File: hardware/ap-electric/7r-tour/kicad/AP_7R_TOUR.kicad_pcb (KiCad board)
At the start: 2 copper layers, 176 x 90 mm, 185 parts, among them J1 KF128-5.08-2P, J11 KF128-5.08-3P, J12 KF128-5.08-3P, J13 KF128-5.08-3P, J14 KF128-5.08-3P, J15 USB-C, J2 KF128-5.08-2P, J3 KF128-5.08-2P, J4 KF128-5.08-2P, J5 KF128-5.08-2P, J6 KF128-5.08-2P, J7 KF128-5.08-2P, J8 KF128-5.08-2P, J9 KF128-5.08-2P, K1 G2RL-1A-E DC24, K2 G2RL-1A-E DC24, K3 G2RL-1A-E DC24, K4 G2RL-1A-E DC24, K5 G2RL-1A-E DC24, K6 G2RL-1A-E DC24, K7 G2RL-1A-E DC24, SW1 DSWB08LHGET, SW8 MODO, SW9 RESET, U1 ULN2003ADR, U10 USBLC6-2SC6, U2 TCA9554PWR, U3 TCA9554PWR, U4 TCA9554PWR, U5 TCA9554PWR, U6 CA-IS3092W, U7 LMR16006XDDC, U8 AP63203WU, U9 ESP32-C3-WROOM-02

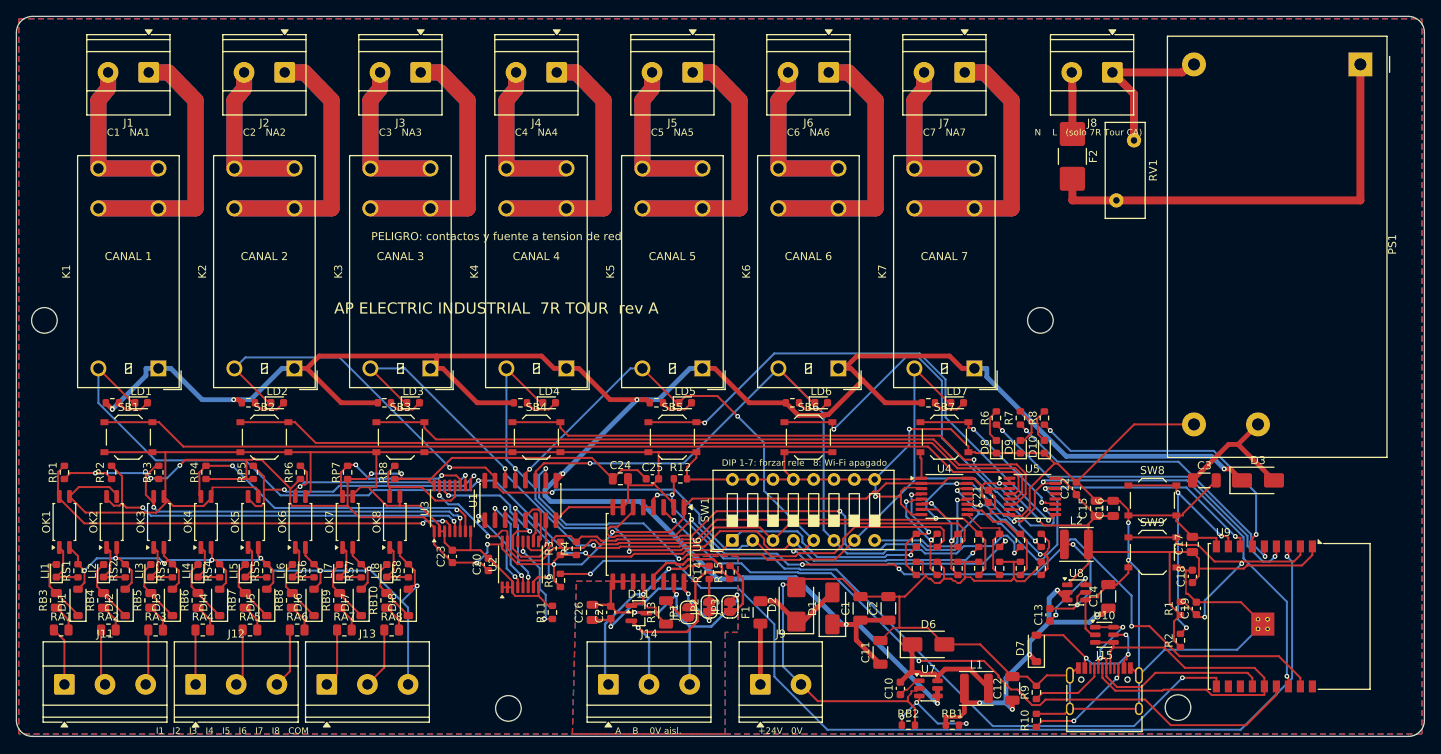
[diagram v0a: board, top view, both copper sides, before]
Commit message: 7R Tour: placa cerrada (DRC 0) y salidas de fabricación por SKU
Ruteo completo con el bus aislado trazado a mano: 0 violaciones,
0 sin conectar, paridad 0, DFM de JLCPCB 0. Gerbers, taladros,
BOM y CPL; BOM/CPL separados para 7R Tour 24DC y 7R Tour CA.
Código verificado del borne KF128-5.08-3P para su huella. LEEME
del 7R Tour con el estado de cierre y los pendientes.

Co-Authored-By: Claude Opus 5.5 <noreply@anthropic.com>
Claude-Session: https://claude.ai/code/session_01WVk3oGwfQfGTmAT2PMp8oW
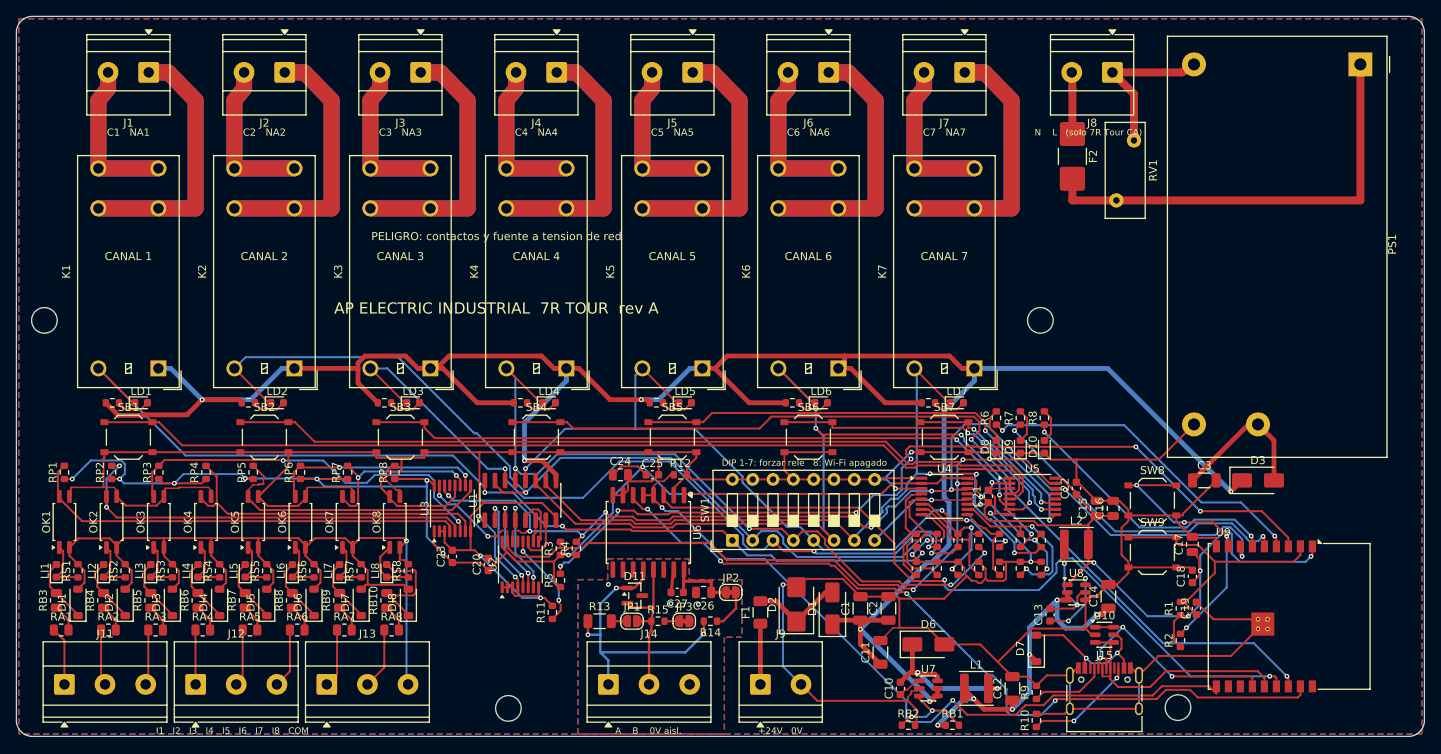
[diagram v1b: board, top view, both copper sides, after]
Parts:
- moved C26 14.1 mm to (185.9, 172.0), turned to 180 degrees
- moved R15 10.9 mm to (180.2, 175.6), turned to 0 degrees
- moved C27 8.67 mm to (182.6, 172.0), turned to 180 degrees
- moved R13 8.37 mm to (172.9, 175.6), turned to 0 degrees
- moved JP1 7.14 mm to (176.9, 175.6), turned to 0 degrees
- moved R14 6.10 mm to (186.8, 175.6), turned to 180 degrees
- moved JP3 6.00 mm to (183.5, 175.6), turned to 0 degrees
- moved JP2 3.24 mm to (189.3, 172.0), turned to 0 degrees
- moved D11 2.26 mm to (177.3, 172.4)
- moved U6 1.50 mm to (179.0, 164.5)
- moved C24 0.50 mm to (175.5, 157.3)
- moved C25 0.50 mm to (179.5, 157.3)
- moved R12 0.50 mm to (183.0, 157.3)
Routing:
- net /GNDB: track 40.7 -> 2.87 mm
- net /USB_DP: track 50.7 -> 30.8 mm
- net /RSB: track 39.3 -> 19.7 mm, vias 1 -> 0
- net /3V3: track 287.8 -> 270.3 mm, vias 11 -> 16
- net /INT: track 124.2 -> 107.6 mm, vias 2 -> 6
- net /BT6: track 54.6 -> 39.6 mm
- net /BOB6: track 94.8 -> 108.5 mm, vias 2 -> 3
- net /VISO: track 22.6 -> 9.46 mm, vias 3 -> 0
- net /COMI: track 109.4 -> 121.1 mm, vias 8 -> 1
- net /SCL: track 142.9 -> 134.3 mm, vias 6 -> 9
- net /RS_TX: track 108.2 -> 99.6 mm
- net /SEN6: track 13.7 -> 21.3 mm, vias 0 -> 2
- net /BT5: track 66.2 -> 59.6 mm
- net /IB8: track 8.18 -> 14.6 mm
- net /BT4: track 70.4 -> 76.5 mm
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
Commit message: 7R Tour rev B: placa ruteada y cerrada (conteo rapido, reloj, puntos de prueba), buscador de caminos para 3 redes largas, BOM/CPL regenerados
Co-Authored-By: Claude Sonnet 5.5 <noreply@anthropic.com>
Claude-Session: https://claude.ai/code/session_01WVk3oGwfQfGTmAT2PMp8oW
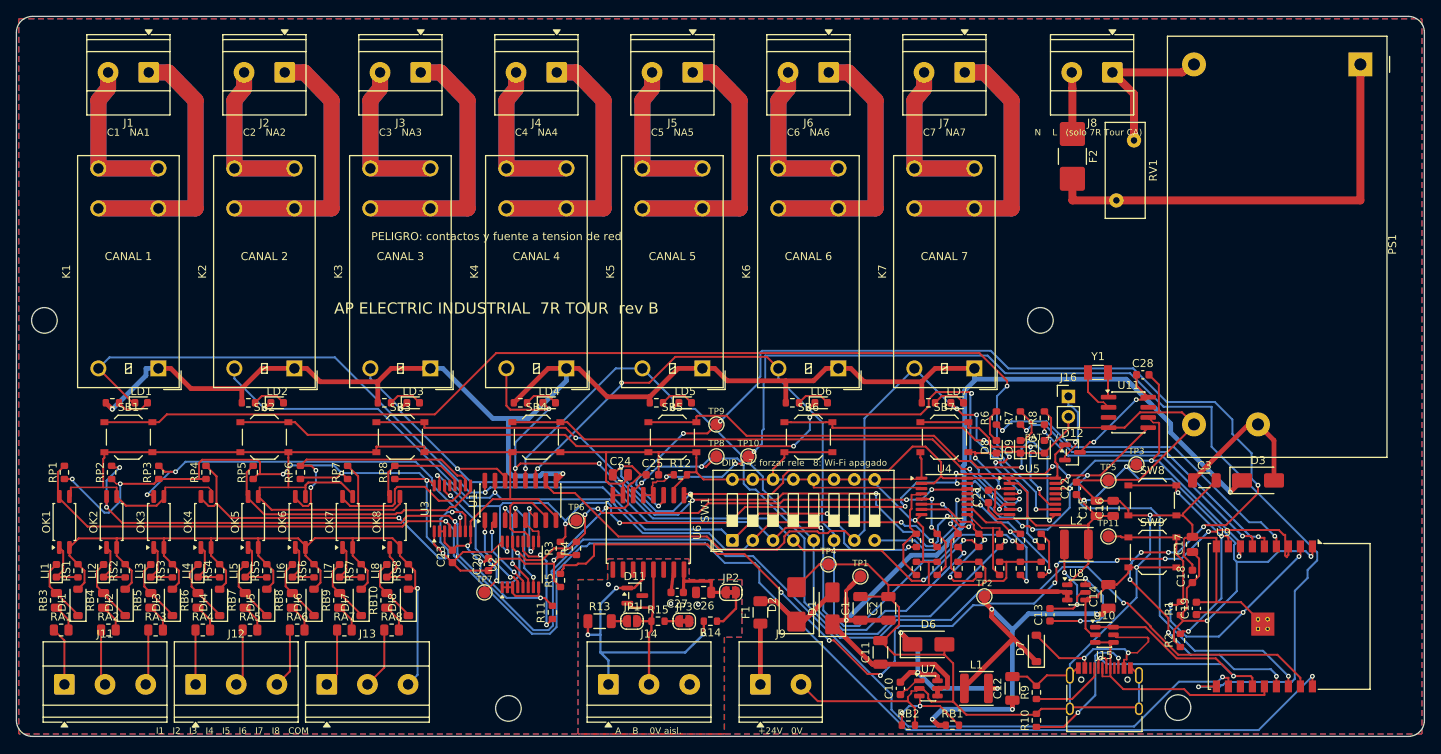
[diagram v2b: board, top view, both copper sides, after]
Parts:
- added C28: 100nF, Capacitor_SMD:C_0603_1608Metric, F.Cu at (240.8, 144.8)
- added D12: BAT54C, Package_TO_SOT_SMD:SOT-23, F.Cu at (232.0, 154.5)
- added J16: BAT, Connector_PinHeader_2.54mm:PinHeader_1x02_P2.54mm_Vertical, F.Cu at (231.5, 147.5)
- added TP1: TP 24V, TestPoint:TestPoint_Pad_D1.5mm, F.Cu at (205.5, 170.0)
- added TP10: TP DE, TestPoint:TestPoint_Pad_D1.5mm, F.Cu at (191.5, 155.0)
- added TP11: TP EN, TestPoint:TestPoint_Pad_D1.5mm, F.Cu at (236.5, 165.0)
- added TP2: TP 5V, TestPoint:TestPoint_Pad_D1.5mm, F.Cu at (221.0, 172.5)
- added TP3: TP 3V3, TestPoint:TestPoint_Pad_D1.5mm, F.Cu at (240.0, 156.0)
- added TP4: TP GND, TestPoint:TestPoint_Pad_D1.5mm, F.Cu at (201.5, 168.5)
- added TP5: TP GND, TestPoint:TestPoint_Pad_D1.5mm, F.Cu at (236.5, 158.0)
- added TP6: TP SDA, TestPoint:TestPoint_Pad_D1.5mm, F.Cu at (170.0, 163.0)
- added TP7: TP SCL, TestPoint:TestPoint_Pad_D1.5mm, F.Cu at (158.5, 172.0)
- added TP8: TP TX, TestPoint:TestPoint_Pad_D1.5mm, F.Cu at (187.5, 155.0)
- added TP9: TP RX, TestPoint:TestPoint_Pad_D1.5mm, F.Cu at (187.5, 151.0)
- added U11: PCF8563T/5,518, Package_SO:SOIC-8_3.9x4.9mm_P1.27mm, F.Cu at (239.0, 149.5)
- added Y1: 32.768kHz 12.5pF, Crystal:Crystal_SMD_3215-2Pin_3.2x1.5mm, F.Cu at (235.2, 144.5)
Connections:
- U9 pad 11: unconnected-(U9-IO20/RXD-Pad11) -> /E2
- U9 pad 18: unconnected-(U9-IO0-Pad18) -> /E1
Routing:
- net /E1: track 55.4 -> 195.8 mm, vias 0 -> 2
- net /E2: track 53.4 -> 182.3 mm, vias 2 -> 4
- net /RS_RX: track 93.4 -> 150.9 mm, vias 2 -> 10
- net /RS_DE: track 93.8 -> 144.8 mm, vias 2 -> 4
- net /3V3: track 270.3 -> 310.2 mm, vias 16 -> 14
- net /GND: track 556.9 -> 594.0 mm, vias 9 -> 8
- net /V5: track 44.9 -> 71.7 mm, vias 6 -> 4
- net /V24: track 301.2 -> 275.5 mm, vias 6 -> 4
- net /BT1: track 120.4 -> 136.8 mm, vias 0 -> 4
- net /BT3: track 85.1 -> 100.0 mm, vias 2 -> 6
- net /EN: track 33.9 -> 48.8 mm, vias 0 -> 3
- net /BOB2: track 118.7 -> 103.8 mm, vias 2 -> 4
- net /VRTC: track 0.00 -> 14.8 mm, vias 0 -> 2
- net /RS_TX: track 99.6 -> 113.9 mm, vias 4 -> 3
- net /SDA: track 152.9 -> 166.2 mm, vias 7 -> 11
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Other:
- board text added: "AP ELECTRIC INDUSTRIAL 7R TOUR rev B"
- board text added: "AP Electric Industrial 7R Tour rev B - CONCEPTO, sin certificar. Desconectar la red antes de abrir."
- board text added: "BAT + / -"
- board text removed: "AP ELECTRIC INDUSTRIAL 7R TOUR rev A"
- board text removed: "AP Electric Industrial 7R Tour rev A - CONCEPTO, sin certificar. Desconectar la red antes de abrir."

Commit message: 7R Tour rev B cerrada con pull-downs RD1-RD7: ERC 0, DRC 0, sin conectar 0, DFM 0; poda de ramas sin salida en ruta_auto; BOM/CPL, renders y vistas regenerados
Co-Authored-By: Claude Sonnet 5.5 <noreply@anthropic.com>
Claude-Session: https://claude.ai/code/session_01WVk3oGwfQfGTmAT2PMp8oW
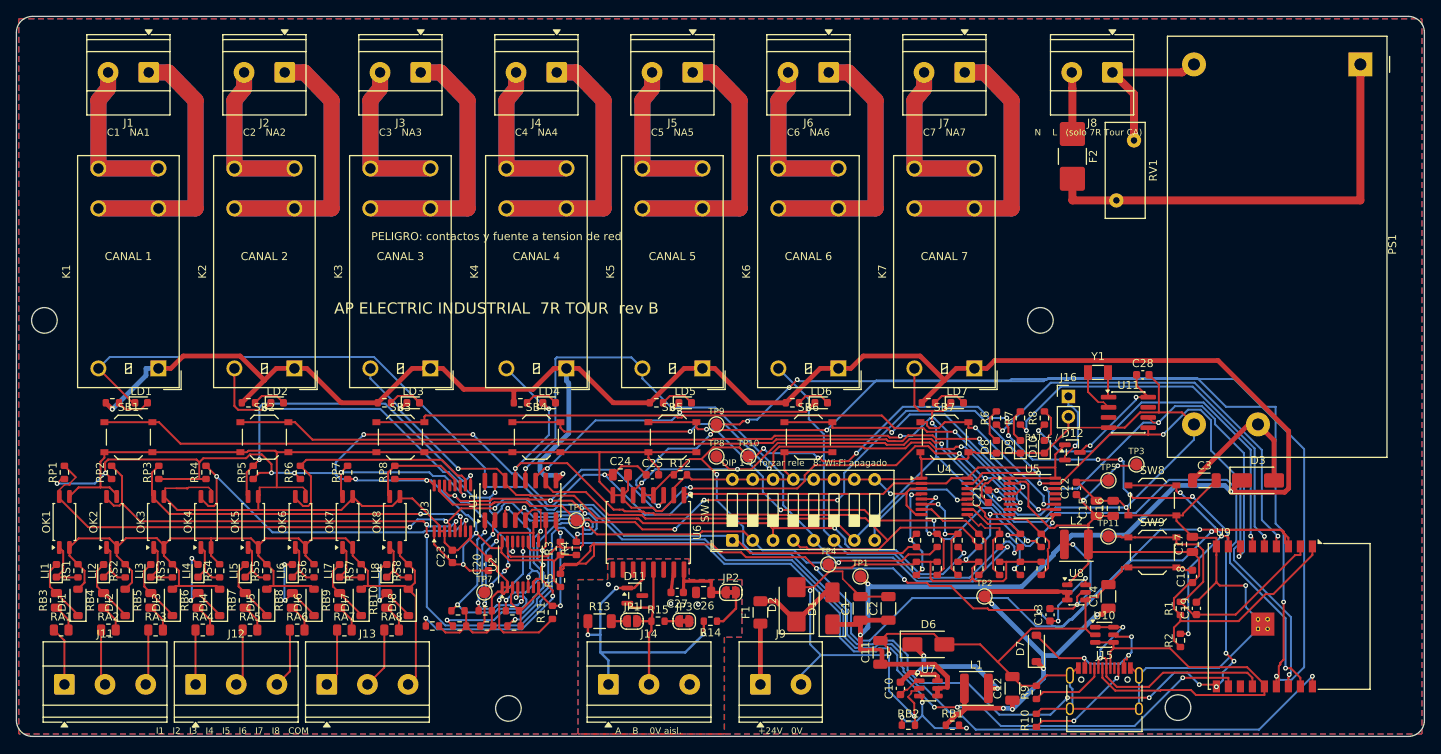
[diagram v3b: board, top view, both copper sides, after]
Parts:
- added RD1: 10k, Resistor_SMD:R_0603_1608Metric, F.Cu at (155.2, 174.3)
- added RD2: 10k, Resistor_SMD:R_0603_1608Metric, F.Cu at (158.6, 174.3)
- added RD3: 10k, Resistor_SMD:R_0603_1608Metric, F.Cu at (162.0, 174.3)
- added RD4: 10k, Resistor_SMD:R_0603_1608Metric, F.Cu at (152.0, 176.2)
- added RD5: 10k, Resistor_SMD:R_0603_1608Metric, F.Cu at (155.4, 176.2)
- added RD6: 10k, Resistor_SMD:R_0603_1608Metric, F.Cu at (158.8, 176.2)
- added RD7: 10k, Resistor_SMD:R_0603_1608Metric, F.Cu at (162.2, 176.2)
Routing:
- net /RS_RX: track 150.9 -> 241.7 mm, vias 10 -> 8
- net /INT: track 115.9 -> 186.4 mm, vias 8 -> 5
- net /RS_DE: track 144.8 -> 197.7 mm, vias 4 -> 16
- net /DO4: track 12.3 -> 49.3 mm, vias 2 -> 4
- net /V24: track 275.5 -> 304.8 mm, vias 4 -> 5
- net /SCL: track 144.8 -> 173.6 mm, vias 13 -> 14
- net /GND: track 594.0 -> 622.2 mm, vias 8 -> 11
- net /DO5: track 3.87 -> 29.8 mm, vias 0 -> 2
- net /USB_DP: track 30.0 -> 50.1 mm
- net /3V3: track 310.2 -> 328.2 mm
- net /BOB3: track 108.9 -> 91.4 mm
- net /V5: track 71.7 -> 55.2 mm, vias 4 -> 5
- net /DO1: track 10.3 -> 25.9 mm, vias 2 -> 3
- net /BT1: track 136.8 -> 121.6 mm, vias 4 -> 2
- net /SDA: track 166.2 -> 179.9 mm, vias 11 -> 7
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
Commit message: Hallazgos del revisor adversarial: entradas desacopladas de fabrica, vigilancia Modbus por cualquier trama, OEE no calculable tras reinicio, clave aleatoria, fabrica completa, fallas I2C con 3 intentos, CPL en las coordenadas de los Gerber, archivos 24DC_solo_SMD, serigrafia NA/C y textos corregidos; estado de cada hallazgo
Co-Authored-By: Claude Sonnet 5.5 <noreply@anthropic.com>
Claude-Session: https://claude.ai/code/session_01WVk3oGwfQfGTmAT2PMp8oW
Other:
- board text added: "NA1 C1"
- board text added: "NA2 C2"
- board text added: "NA3 C3"
- board text added: "NA4 C4"
- board text added: "NA5 C5"
- board text added: "NA6 C6"
- board text added: "NA7 C7"
- board text removed: "C1 NA1"
- board text removed: "C2 NA2"
- board text removed: "C3 NA3"
- board text removed: "C4 NA4"
- board text removed: "C5 NA5"
- board text removed: "C6 NA6"
- board text removed: "C7 NA7"

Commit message: Segunda ronda de correcciones: ciclo nominal en PK ENT, fallas I2C separadas, FABRICA solo local y con maniobras conservadas, consola USB con lineas completas, clave con ruido de hardware, vigilancia como latido de escrituras; web sin falsas promesas, datos malformados, doble envio, estados unificados, 30 V, contraste; consola con indicador de datos viejos y confirmaciones; AP Studio con clave; C14 a 10uF 50V
Co-Authored-By: Claude Sonnet 5.5 <noreply@anthropic.com>
Claude-Session: https://claude.ai/code/session_01WVk3oGwfQfGTmAT2PMp8oW
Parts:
- C14: value 10uF 25V -> 10uF 50V
